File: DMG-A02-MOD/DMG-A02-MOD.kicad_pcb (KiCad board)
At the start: 2 copper layers, 51 x 60.7 mm, 16 parts, among them U0 CartBus, U1 SSOP-32_MROM, U2 LQFP-32_MBC, U3 SOIC-28_SRAM, U4 TSOP-6_1.65x3.05mm_P0.95mm

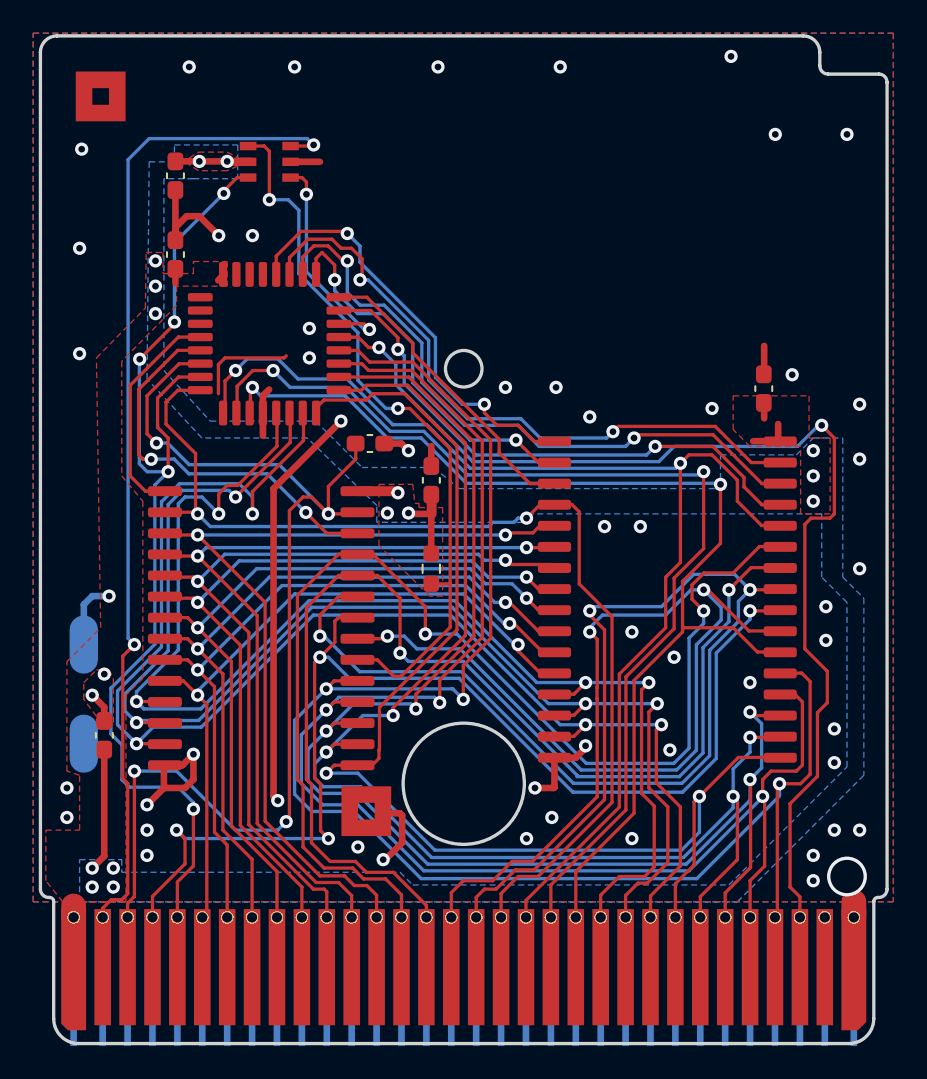
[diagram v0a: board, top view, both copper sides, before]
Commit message: Update A02 to REV2
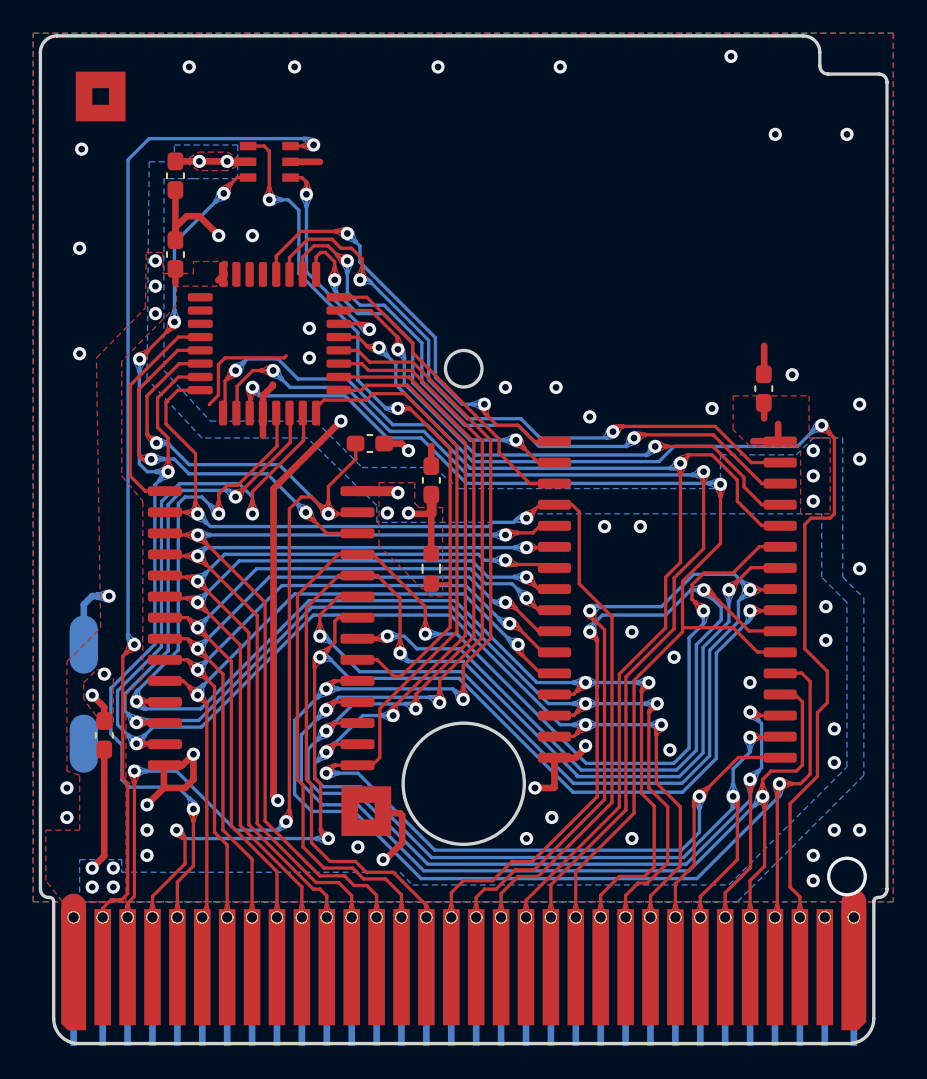
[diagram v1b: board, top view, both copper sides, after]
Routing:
- net GND: track 68.6 -> 69.9 mm
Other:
- board text added: "F-RAM MOD BOARD REV2"
- board text removed: "F-RAM MOD BOARD REV1"
